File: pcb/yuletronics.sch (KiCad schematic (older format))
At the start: 52 parts, among them IC1 STM32F042F6P6, IC3 TLV61225, J1 BATT, J2 MICROUSB, J3 CONN_01x08, P1 SWD_TC, SW1 BOOTLOAD, SW2 PWR_SWITCH, SW3 BOOTLOAD, U1 XC6210B332MR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

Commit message: Update LED farnell code, generate BOM
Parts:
- C1, C4, C7: value 10µ -> 10u
- C5, C6: value 1µ -> 1u; Digikey Value -> (none); Fieldname Value -> (none)
- D1, D2: renamed from D?; Digikey Value -> (none); Fieldname Value -> (none)
- D10, D13, D14, D3, D5, D6: Digikey Value -> (none); Farnell 2093940 -> 1855553; Fieldname Value -> (none)
- J3, R12, R15, R17, R18, R20, R21, R23, R24, R26, R29, R32, R35, R36, R38, R39, R41, R42, R7, SW1, SW3, U1, U2, X1: Digikey Value -> (none); Fieldname Value -> (none)
- L1: value 4µ7 -> 4u7
- R5, R6: renamed from R?; Digikey Value -> (none); Fieldname Value -> (none)

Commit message: Tidy BOM
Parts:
- J3, X1: Farnell Value -> (none)
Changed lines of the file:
@@
 F 2 "yule:Interboard" H 9000 3000 50  0001 C CNN
 F 3 "" H 9000 3000 50  0001 C CNN
-F 4 "Value" H 9000 3000 60  0001 C CNN "Farnell"
 	1    9000 3000
 	1    0    0    -1
@@
 F 2 "yule:tree_silk_scaled" H 6050 5900 50  0001 C CNN
 F 3 "" H 6050 5900 50  0001 C CNN
-F 4 "Value" H 6050 5900 60  0001 C CNN "Farnell"
 	1    6050 5900
 	1    0    0    -1

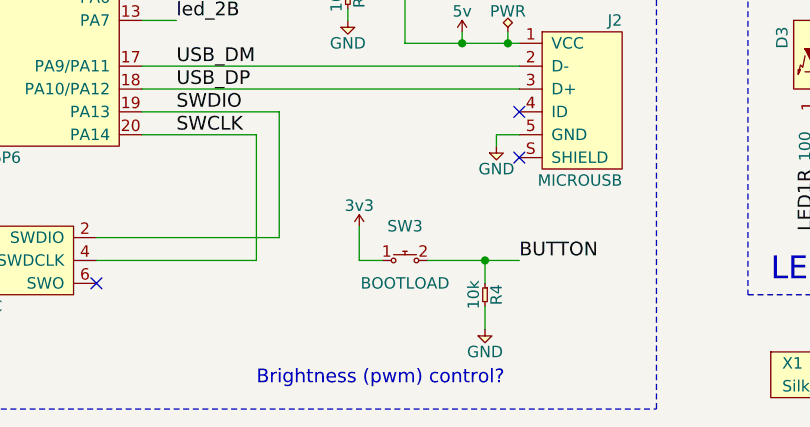
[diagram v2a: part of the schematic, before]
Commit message: First iteration of led threads complete
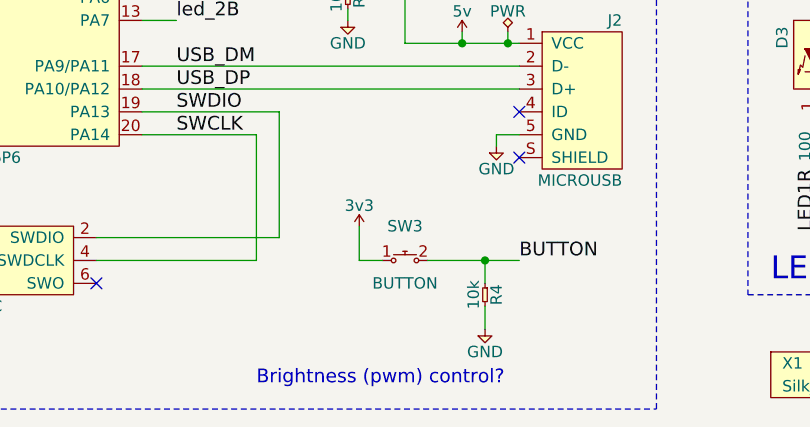
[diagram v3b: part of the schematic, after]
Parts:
- SW3: value BOOTLOAD -> BUTTON
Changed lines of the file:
@@
 P 4450 5350
 F 0 "SW3" H 4450 5500 50  0000 C CNN
-F 1 "BOOTLOAD" H 4450 5250 50  0000 C CNN
+F 1 "BUTTON" H 4450 5250 50  0000 C CNN
 F 2 "yule:MOM_SWITCH" H 4450 5350 50  0001 C CNN
 F 3 "http://www.farnell.com/datasheets/1582297.pdf" H 4450 5350 50  0001 C CNN
